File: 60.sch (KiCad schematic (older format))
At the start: 153 parts, among them K1 KEYSW, K10 KEYSW, K11 KEYSW, K12 KEYSW, K13 KEYSW, K14 KEYSW, K15 KEYSW, K16 KEYSW, K17 KEYSW, K18 KEYSW, K19 KEYSW, K2 KEYSW, K20 KEYSW, K21 KEYSW, K22 KEYSW, K23 KEYSW, K24 KEYSW, K25 KEYSW, K26 KEYSW, K27 KEYSW, K28 KEYSW, K29 KEYSW, K3 KEYSW, K30 KEYSW, K31 KEYSW, K32 KEYSW, K33 KEYSW, K34 KEYSW, K35 KEYSW, K36 KEYSW, K37 KEYSW, K38 KEYSW, K39 KEYSW, K4 KEYSW, K40 KEYSW, K41 KEYSW, K42 KEYSW, K43 KEYSW, K44 KEYSW, K45 KEYSW, K46 KEYSW, K47 KEYSW, K48 KEYSW, K49 KEYSW, K5 KEYSW, K50 KEYSW, K51 KEYSW, K52 KEYSW, K53 KEYSW, K54 KEYSW, K55 KEYSW, K56 KEYSW, K57 KEYSW, K58 KEYSW, K59 KEYSW, K6 KEYSW, K60 KEYSW, K61 KEYSW, K62 KEYSW, K63 KEYSW, K64 KEYSW, K65 KEYSW, K66 KEYSW, K67 KEYSW, K68 KEYSW, K69 KEYSW, K7 KEYSW, K70 KEYSW, K71 KEYSW, K72 KEYSW, K73 KEYSW, K74 KEYSW, K75 KEYSW, K76 KEYSW, K77 KEYSW, K78 KEYSW, K79 KEYSW, K8 KEYSW, K80 KEYSW, K81 KEYSW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

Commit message: pre-diode swap
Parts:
- added BT1: Battery, Battery_Holders:Keystone_1058_1x2032-CoinCell, symbol Battery
- added C1, C2, C3, C4: 0.1u, Capacitors_SMD:C_0805_HandSoldering, symbol C
- added C5: 1u, Capacitors_SMD:C_0805_HandSoldering, symbol C
- added D67: D_Schottky_x2_KCom_AAK, TO_SOT_Packages_SMD:SOT-23_Handsoldering, symbol D_Schottky_x2_KCom_AAK
- added IC1: ATXMEGA32A4U-A, Housings_QFP:TQFP-44_10x10mm_Pitch0.8mm, symbol ATXMEGA32A4U-A
- added J1: USB_mini_micro_B, symbol USB_mini_micro_B
- added P1: CONN_01X01, Connectors_TestPoints:Test_Point_Pad_d2.5mm, symbol CONN_01X01
- added R1: 10k, Resistors_SMD:R_0805_HandSoldering, symbol R
- added R2, R3: 22, Resistors_SMD:R_0805_HandSoldering, symbol R
- added R4, R5: 100k, Resistors_SMD:R_0805_HandSoldering, symbol R
- added SW1: SW_PUSH, Cartel:c&k_PTS645SH50SMTR92_LFS, symbol SW_PUSH
- added U1: nRF24L01+, Cartel:nRF24L01+_SMD, symbol nRF24L01+
- added U2: MCP1700T-3002E/TT, TO_SOT_Packages_SMD:SOT-23_Handsoldering, symbol MCP1700T-3002E/TT
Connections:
- net labels added: +3.3V, +5V, COL0, COL1, COL10, COL11, COL12, COL13, COL14, COL2, COL3, COL4, COL5, COL6, COL7, COL8, COL9, D+, D-, GND, ROW0, ROW1, ROW2, ROW3, ROW4
- wire segments 196 -> 239
- no-connect marks 0 -> 9

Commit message: Finished PCB functionality
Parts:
- added D68, D69: 1N4148, Diodes_SMD:D_SOD-323_HandSoldering, symbol D
- added K88, K93, K96: KEYSW, MXAlps:MX-2.75U-ReversedStabilizer-NoLED, symbol KEYSW
- added K89, K92: KEYSW, MXAlps:MX-1.25U-NoLED, symbol KEYSW
- added K90, K91, K94: KEYSW, MXAlps:MX-2.25U-ReversedStabilizer-NoLED, symbol KEYSW
- added K95: KEYSW, MXAlps:MX-2U-ReversedStabilizers-NoLED, symbol KEYSW
- D1, D10, D11, D12, D13, D14, D15, D16, D17, D18, D19, D2, D20, D21, D22, D23, D24, D25, D26, D27, D28, D29, D3, D30, D31, D32, D33, D34, D35, D36, D37, D38, D39, D4, D40, D41, D42, D43, D44, D45, D46, D47, D48, D49, D5, D50, D51, D52, D53, D54, D55, D56, D57, D58, D59, D6, D60, D61, D62, D63, D64, D65, D66, D7, D8, D9: footprint Cartel:combo_diode -> Diodes_SMD:D_SOD-323_HandSoldering
- J1: footprint (none) -> keyboard_parts:USB_miniB_hirose_5S8
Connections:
- wire segments 239 -> 249
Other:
- moved on the sheet: K71, K79

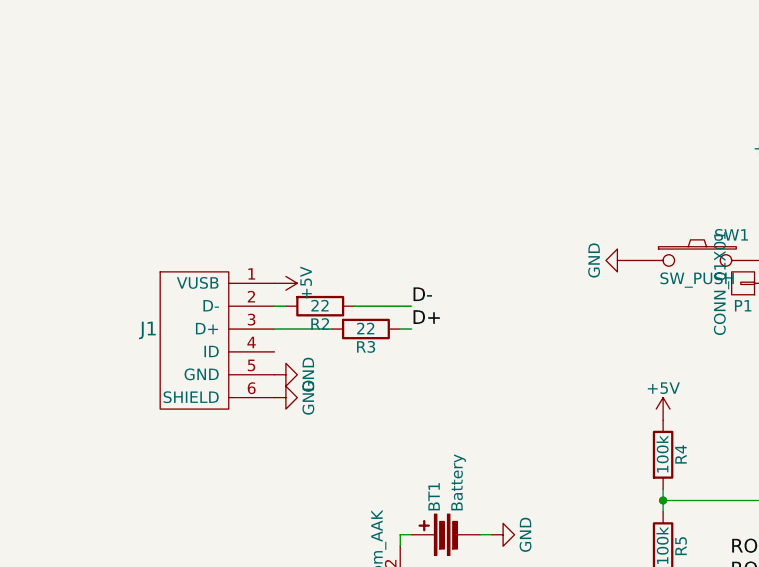
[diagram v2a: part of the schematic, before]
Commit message: Add fuse
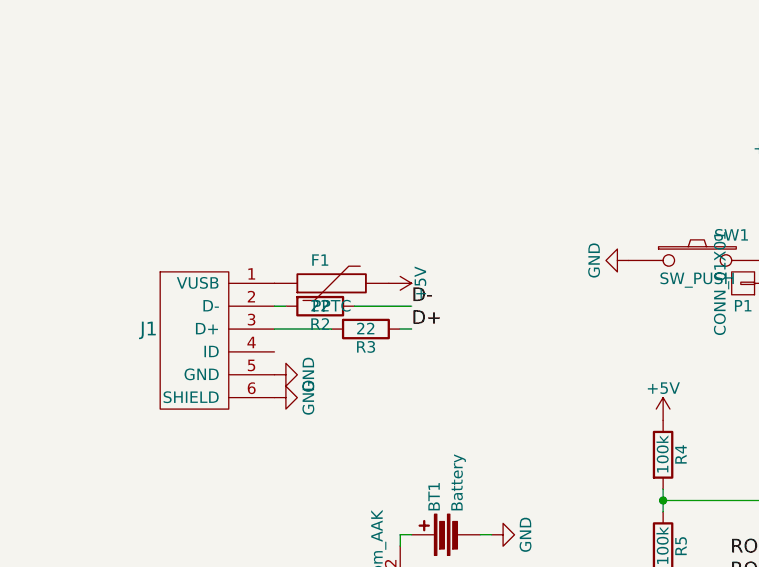
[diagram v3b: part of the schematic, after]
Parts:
- added F1: PPTC, Fuse_Holders_and_Fuses:Fuse_SMD1206_HandSoldering, symbol PPTC
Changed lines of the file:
@@
 L +5V #PWR01
 U 1 1 59F4BFAA
-P 1300 4900
-F 0 "#PWR01" H 1300 4750 50  0001 C CNN
-F 1 "+5V" H 1300 5040 50  0000 C CNN
-F 2 "" H 1300 4900 50  0000 C CNN
-F 3 "" H 1300 4900 50  0000 C CNN
-	1    1300 4900
+P 1800 4900
+F 0 "#PWR01" H 1800 4750 50  0001 C CNN
+F 1 "+5V" H 1800 5040 50  0000 C CNN
+F 2 "" H 1800 4900 50  0000 C CNN
+F 3 "" H 1800 4900 50  0000 C CNN
+	1    1800 4900
 	0    1    1    0
 $EndComp
@@
 	1    0    0    -1
 $EndComp
+$Comp
+L PPTC F1
+U 1 1 59F5D068
+P 1550 4900
+F 0 "F1" H 1500 5000 50  0000 C CNN
+F 1 "PPTC" H 1550 4800 50  0000 C CNN
+F 2 "Fuse_Holders_and_Fuses:Fuse_SMD1206_HandSoldering" V 1550 4900 60  0001 C CNN
+F 3 "" V 1550 4900 60  0000 C CNN
+	1    1550 4900
+	1    0    0    -1
+$EndComp

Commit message: Prototype 1
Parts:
- removed F1: PPTC, Fuse_Holders_and_Fuses:Fuse_SMD1206_HandSoldering, symbol PPTC
- removed P1: CONN_01X01, Connectors_TestPoints:Test_Point_Pad_d2.5mm, symbol CONN_01X01
- removed R2, R3: 22, Resistors_SMD:R_0805_HandSoldering, symbol R
- added C6: 0.1uF, Capacitors_SMD:C_0805_HandSoldering, symbol C
- added P1: TC2030-MCP-NL, Tag-Connect:TC2030-MCP-NL, symbol TC2030-MCP-NL
- added SJ1: SOLDER_JUMPER, keyboard_parts:SOLDER_JUMPER_2, symbol SOLDER_JUMPER
- added SW2: POWER, Pin_Headers:Pin_Header_Straight_1x02_Pitch2.54mm, symbol SW_PUSH
- BT1: footprint Battery_Holders:Keystone_1058_1x2032-CoinCell -> lib:CR2032_BK-913
- D67: value D_Schottky_x2_KCom_AAK -> BAT54C-7-F
- SW1: footprint Cartel:c&k_PTS645SH50SMTR92_LFS -> Buttons_Switches_SMD:SW_SPST_TL3342
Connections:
- net labels added: PDI, PDI_CLK
- wire segments 249 -> 262
- no-connect marks 9 -> 5
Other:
- moved on the sheet: BT1

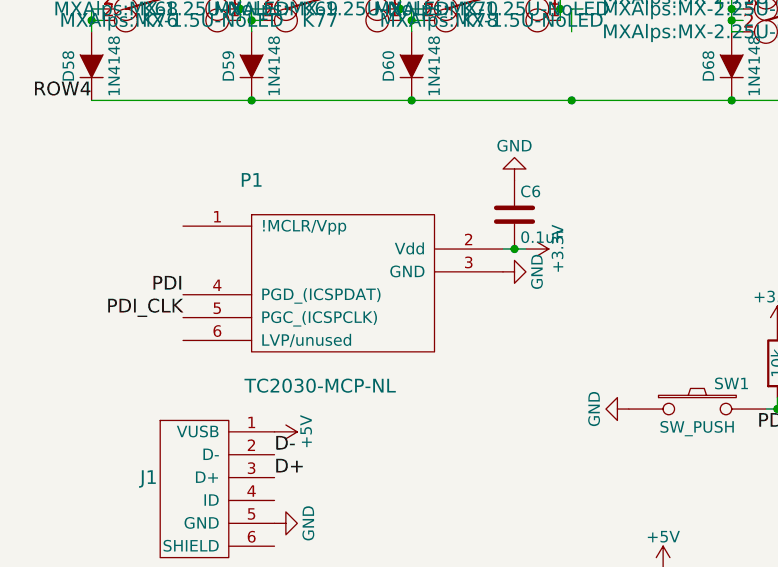
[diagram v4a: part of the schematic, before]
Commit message: Prototype 1 fix
Fix tag connect and added airi
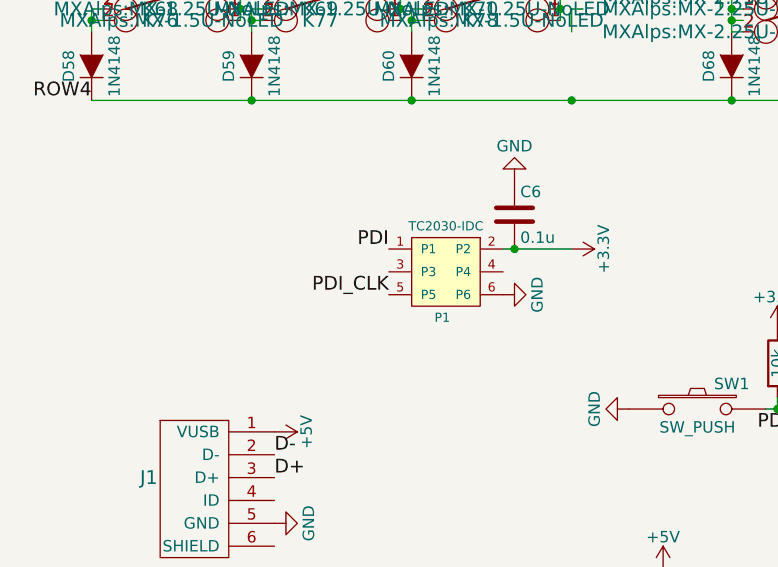
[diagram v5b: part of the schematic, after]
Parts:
- removed P1: TC2030-MCP-NL, Tag-Connect:TC2030-MCP-NL, symbol TC2030-MCP-NL
- added P1: TC2030-IDC, Tag-Connect:TC2030-NL_SMALL, symbol TC2030-IDC
- C6: value 0.1uF -> 0.1u
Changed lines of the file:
@@
 $EndComp
 $Comp
-L +5V #PWR01
+L +5V #PWR9
 U 1 1 59F4BFAA
 P 1300 4900
-F 0 "#PWR01" H 1300 4750 50  0001 C CNN
+F 0 "#PWR9" H 1300 4750 50  0001 C CNN
 F 1 "+5V" H 1300 5040 50  0000 C CNN
 F 2 "" H 1300 4900 50  0000 C CNN
@@
 $EndComp
 $Comp
-L GND #PWR02
+L GND #PWR10
 U 1 1 59F4C0F2
 P 1300 5300
-F 0 "#PWR02" H 1300 5050 50  0001 C CNN
+F 0 "#PWR10" H 1300 5050 50  0001 C CNN
 F 1 "GND" H 1300 5150 50  0000 C CNN
 F 2 "" H 1300 5300 50  0000 C CNN
@@
 $EndComp
 $Comp
-L +5V #PWR03
+L +5V #PWR17
 U 1 1 59F5069E
 P 800 6900
-F 0 "#PWR03" H 800 6750 50  0001 C CNN
+F 0 "#PWR17" H 800 6750 50  0001 C CNN
 F 1 "+5V" H 800 7040 50  0000 C CNN
 F 2 "" H 800 6900 50  0000 C CNN
@@
 $EndComp
 $Comp
-L GND #PWR04
+L GND #PWR19
 U 1 1 59F50FE5
 P 1200 7300
-F 0 "#PWR04" H 1200 7050 50  0001 C CNN
+F 0 "#PWR19" H 1200 7050 50  0001 C CNN
 F 1 "GND" H 1200 7150 50  0000 C CNN
 F 2 "" H 1200 7300 50  0000 C CNN
@@
 $EndComp
 $Comp
-L GND #PWR05
+L GND #PWR20
 U 1 1 59F513C7
 P 1650 7300
-F 0 "#PWR05" H 1650 7050 50  0001 C CNN
+F 0 "#PWR20" H 1650 7050 50  0001 C CNN
 F 1 "GND" H 1650 7150 50  0000 C CNN
 F 2 "" H 1650 7300 50  0000 C CNN
@@
 	1850 5800 1850 6050
 $Comp
-L GND #PWR06
+L GND #PWR12
 U 1 1 59F536BA
 P 2850 6000
-F 0 "#PWR06" H 2850 5750 50  0001 C CNN
+F 0 "#PWR12" H 2850 5750 50  0001 C CNN
 F 1 "GND" H 2850 5850 50  0000 C CNN
 F 2 "" H 2850 6000 50  0000 C CNN
@@
 $EndComp
 $Comp
-L +3.3V #PWR07
+L +3.3V #PWR16
 U 1 1 59F549B4
 P 2050 6350
-F 0 "#PWR07" H 2050 6200 50  0001 C CNN
+F 0 "#PWR16" H 2050 6200 50  0001 C CNN
 F 1 "+3.3V" H 2050 6490 50  0000 C CNN
 F 2 "" H 2050 6350 50  0000 C CNN
@@
 $EndComp
 $Comp
-L +3.3V #PWR08
+L +3.3V #PWR5
 U 1 1 59F56F19
 P 4350 4400
-F 0 "#PWR08" H 4350 4250 50  0001 C CNN
+F 0 "#PWR5" H 4350 4250 50  0001 C CNN
 F 1 "+3.3V" H 4350 4540 50  0000 C CNN
 F 2 "" H 4350 4400 50  0000 C CNN
@@
 $EndComp
 $Comp
-L +3.3V #PWR09
+L +3.3V #PWR6
 U 1 1 59F59202
 P 3500 4450
-F 0 "#PWR09" H 3500 4300 50  0001 C CNN
+F 0 "#PWR6" H 3500 4300 50  0001 C CNN
 F 1 "+3.3V" H 3500 4590 50  0000 C CNN
 F 2 "" H 3500 4450 50  0000 C CNN
@@
 Connection ~ 3500 4800
 $Comp
-L GND #PWR010
+L GND #PWR8
 U 1 1 59F59982
 P 2850 4800
-F 0 "#PWR010" H 2850 4550 50  0001 C CNN
+F 0 "#PWR8" H 2850 4550 50  0001 C CNN
 F 1 "GND" H 2850 4650 50  0000 C CNN
 F 2 "" H 2850 4800 50  0000 C CNN
@@
 D-
 $Comp
-L GND #PWR011
+L GND #PWR18
 U 1 1 59F5B08C
 P 4300 7200
-F 0 "#PWR011" H 4300 6950 50  0001 C CNN
+F 0 "#PWR18" H 4300 6950 50  0001 C CNN
 F 1 "GND" H 4300 7050 50  0000 C CNN
 F 2 "" H 4300 7200 50  0000 C CNN
@@
 	5700 6400 5900 6400
 $Comp
-L GND #PWR012
+L GND #PWR15
 U 1 1 59F5FC8B
 P 5900 6200
-F 0 "#PWR012" H 5900 5950 50  0001 C CNN
+F 0 "#PWR15" H 5900 5950 50  0001 C CNN
 F 1 "GND" H 5900 6050 50  0000 C CNN
 F 2 "" H 5900 6200 50  0000 C CNN
@@
 $EndComp
 $Comp
-L +3.3V #PWR013
+L +3.3V #PWR13
 U 1 1 59F5FDE7
 P 5900 6100
-F 0 "#PWR013" H 5900 5950 50  0001 C CNN
+F 0 "#PWR13" H 5900 5950 50  0001 C CNN
 F 1 "+3.3V" H 5900 6240 50  0000 C CNN
 F 2 "" H 5900 6100 50  0000 C CNN
@@
 Connection ~ 6050 4000
 $Comp
-L +3.3V #PWR014
+L +3.3V #PWR2
 U 1 1 59F6659B
 P 5550 3950
-F 0 "#PWR014" H 5550 3800 50  0001 C CNN
+F 0 "#PWR2" H 5550 3800 50  0001 C CNN
 F 1 "+3.3V" H 5550 4090 50  0000 C CNN
 F 2 "" H 5550 3950 50  0000 C CNN
@@
 Connection ~ 5550 4400
 $Comp
-L GND #PWR015
+L GND #PWR7
 U 1 1 59F69B28
 P 5550 4450
-F 0 "#PWR015" H 5550 4200 50  0001 C CNN
+F 0 "#PWR7" H 5550 4200 50  0001 C CNN
 F 1 "GND" H 5550 4300 50  0000 C CNN
 F 2 "" H 5550 4450 50  0000 C CNN
@@
 Connection ~ 3000 5850
 $Comp
-L +5V #PWR016
+L +5V #PWR11
 U 1 1 59F7C485
 P 3000 5500
-F 0 "#PWR016" H 3000 5350 50  0001 C CNN
+F 0 "#PWR11" H 3000 5350 50  0001 C CNN
 F 1 "+5V" H 3000 5640 50  0000 C CNN
 F 2 "" H 3000 5500 50  0000 C CNN
@@
 $EndComp
 $Comp
-L GND #PWR017
+L GND #PWR14
 U 1 1 59F7C5ED
 P 3000 6200
-F 0 "#PWR017" H 3000 5950 50  0001 C CNN
+F 0 "#PWR14" H 3000 5950 50  0001 C CNN
 F 1 "GND" H 3000 6050 50  0000 C CNN
 F 2 "" H 3000 6200 50  0000 C CNN
@@
 Wire Wire Line
 	2550 5800 2550 6000
-$Comp
-L TC2030-MCP-NL P1
-U 1 1 5A5ABE18
-P 1200 4000
-F 0 "P1" H 1200 4200 60  0000 C CNN
-F 1 "TC2030-MCP-NL" H 1500 3300 60  0000 C CNN
-F 2 "Tag-Connect:TC2030-MCP-NL" H 1200 4000 60  0001 C CNN
-F 3 "" H 1200 4000 60  0000 C CNN
-	1    1200 4000
-	1    0    0    -1
-$EndComp
-$Comp
-L +3.3V #PWR018
-U 1 1 5A5AC4C8
-P 2400 4100
-F 0 "#PWR018" H 2400 3950 50  0001 C CNN
-F 1 "+3.3V" H 2400 4240 50  0000 C CNN
-F 2 "" H 2400 4100 50  0000 C CNN
-F 3 "" H 2400 4100 50  0000 C CNN
-	1    2400 4100
-	0    1    1    0
-$EndComp
-$Comp
-L GND #PWR019
-U 1 1 5A5AC64E
-P 2300 4200
-F 0 "#PWR019" H 2300 3950 50  0001 C CNN
-F 1 "GND" H 2300 4050 50  0000 C CNN
-F 2 "" H 2300 4200 50  0000 C CNN
-F 3 "" H 2300 4200 50  0000 C CNN
-	1    2300 4200
-	0    -1   -1   0
-$EndComp
-Text Label 900  4300 2    60   ~ 0
-PDI
-Text Label 900  4400 2    60   ~ 0
-PDI_CLK
 Text Label 3650 4500 0    60   ~ 0
 PDI_CLK
@@
 PDI
 $Comp
-L C C6
-U 1 1 5A5B3837
-P 2350 3950
-F 0 "C6" H 2375 4050 50  0000 L CNN
-F 1 "0.1uF" H 2375 3850 50  0000 L CNN
-F 2 "Capacitors_SMD:C_0805_HandSoldering" H 2388 3800 50  0001 C CNN
-F 3 "" H 2350 3950 50  0000 C CNN
-	1    2350 3950
-	1    0    0    -1
-$EndComp
-Wire Wire Line
-	2300 4100 2400 4100
-Connection ~ 2350 4100
-$Comp
-L GND #PWR020
+L GND #PWR1
 U 1 1 5A5B4C28
 P 2350 3800
-F 0 "#PWR020" H 2350 3550 50  0001 C CNN
+F 0 "#PWR1" H 2350 3550 50  0001 C CNN
 F 1 "GND" H 2350 3650 50  0000 C CNN
 F 2 "" H 2350 3800 50  0000 C CNN
@@
 	-1   0    0    1
 $EndComp
+Connection ~ 2350 4100
+Wire Wire Line
+	2300 4100 2600 4100
+$Comp
+L C C6
+U 1 1 5A5B3837
+P 2350 3950
+F 0 "C6" H 2375 4050 50  0000 L CNN
+F 1 "0.1u" H 2375 3850 50  0000 L CNN
+F 2 "Capacitors_SMD:C_0805_HandSoldering" H 2388 3800 50  0001 C CNN
+F 3 "" H 2350 3950 50  0000 C CNN
+	1    2350 3950
+	1    0    0    -1
+$EndComp
+$Comp
+L TC2030-IDC P1
+U 1 1 5A5A4598
+P 2050 4200
+F 0 "P1" H 2000 4000 40  0000 L CNN
+F 1 "TC2030-IDC" H 2050 4400 40  0000 C CNN
+F 2 "Tag-Connect:TC2030-NL_SMALL" H 2050 4200 60  0001 C CNN
+F 3 "" H 2050 4200 60  0000 C CNN
+	1    2050 4200
+	1    0    0    -1
+$EndComp
+$Comp
+L +3.3V #PWR3
+U 1 1 5A5A495C
+P 2600 4100
+F 0 "#PWR3" H 2600 3950 50  0001 C CNN
+F 1 "+3.3V" H 2600 4240 50  0000 C CNN
+F 2 "" H 2600 4100 50  0000 C CNN
+F 3 "" H 2600 4100 50  0000 C CNN
+	1    2600 4100
+	0    1    1    0
+$EndComp
+$Comp
+L GND #PWR4
+U 1 1 5A5A4E0D
+P 2300 4300
+F 0 "#PWR4" H 2300 4050 50  0001 C CNN
+F 1 "GND" H 2300 4150 50  0000 C CNN
+F 2 "" H 2300 4300 50  0000 C CNN
+F 3 "" H 2300 4300 50  0000 C CNN
+	1    2300 4300
+	0    -1   -1   0
+$EndComp
+Text Label 1800 4100 2    60   ~ 0
+PDI
+Text Label 1800 4300 2    60   ~ 0
+PDI_CLK
 $EndSCHEMATC
